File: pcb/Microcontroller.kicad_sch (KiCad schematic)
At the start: 36 parts, among them J1 ISP, Q2 BC817, Q3 BC817, Q4 BC817, SW2 RESET, SW3 START, SW4 STOP, U4 ATmega328P-A, Y1 15MHz

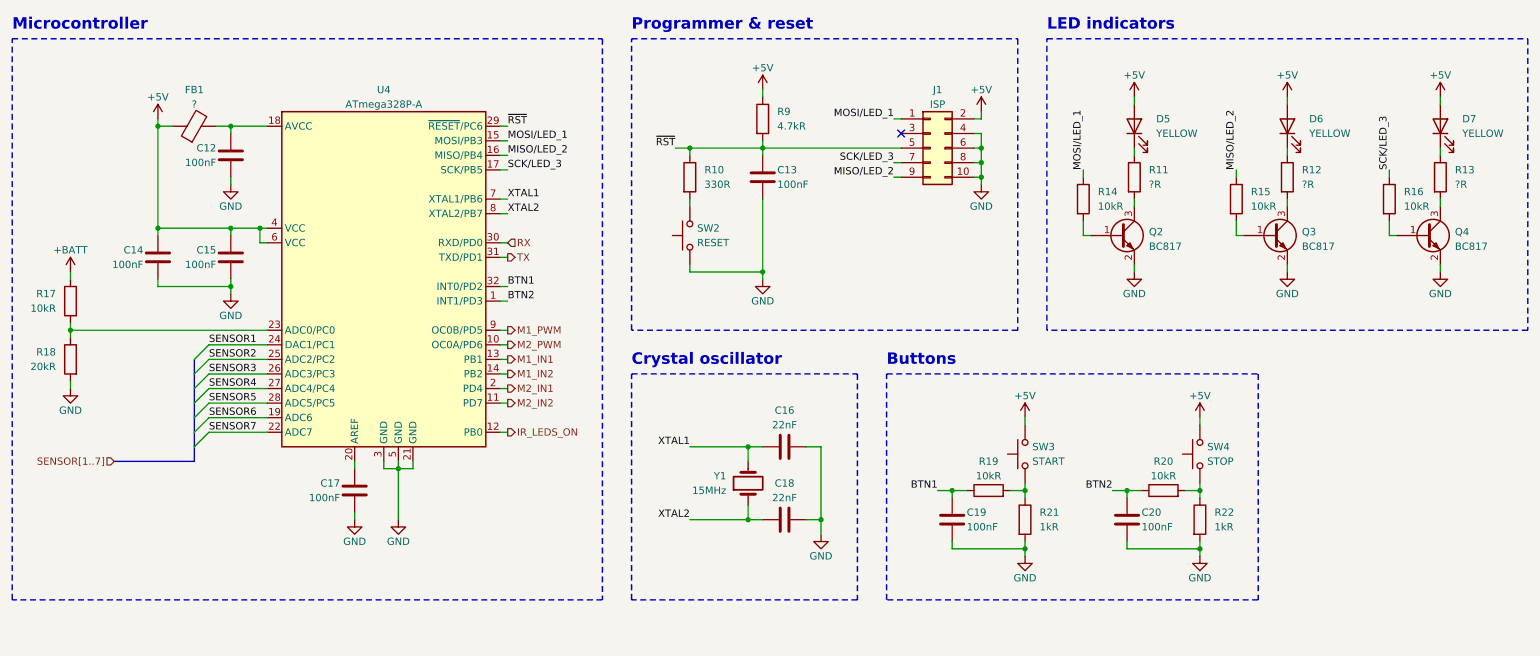
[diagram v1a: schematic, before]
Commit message: [pcb] Schematic clean-up
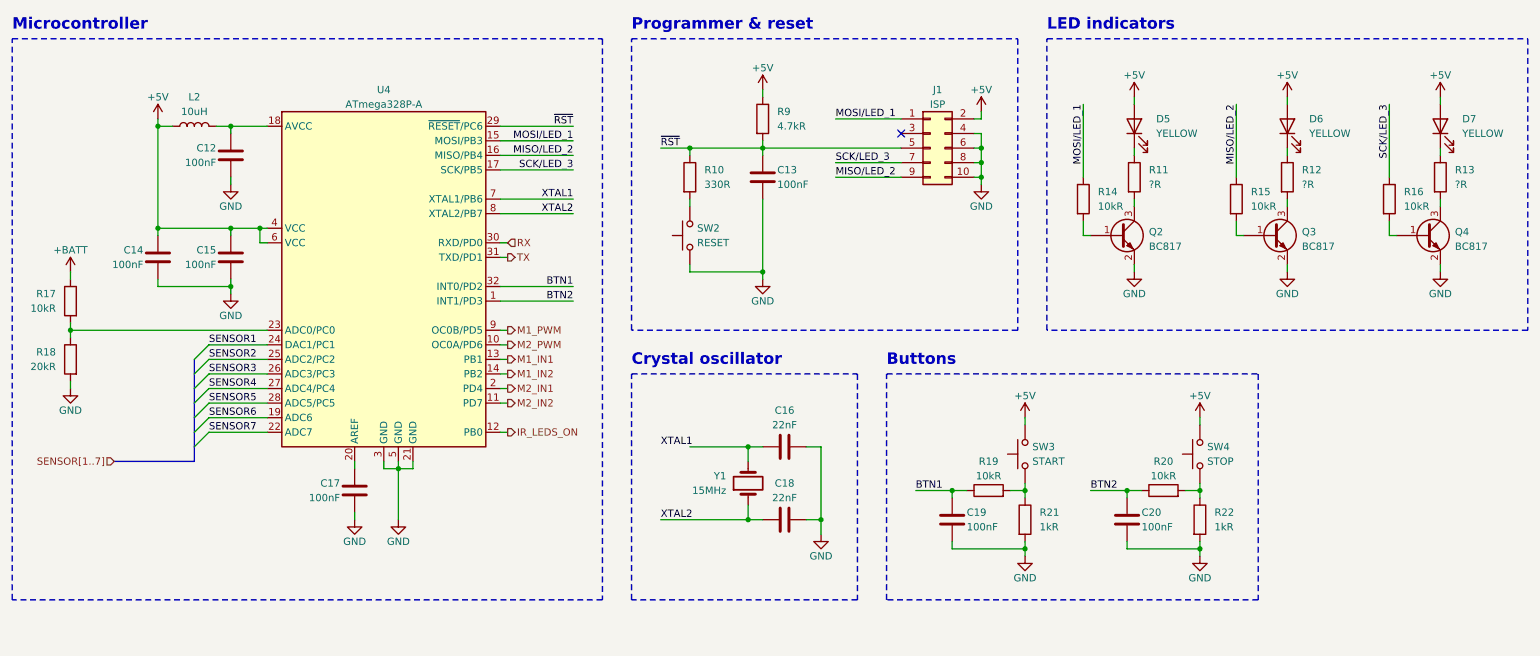
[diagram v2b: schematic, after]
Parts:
- removed FB1: ?, symbol Device:FerriteBead
- added L2: 10uH, symbol Device:L
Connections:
- net +5V: now also L2.1
- net XTAL1: no longer C16.1, Y1.2
- net at C12.1, U4.18 (AVCC): now also L2.2
- new net: C16.1, Y1.2

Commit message: [pcb] Footprints assigned
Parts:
- C12, C13, C14, C15, C16, C17, C18, C19, C20: footprint (none) -> Capacitor_SMD:C_0805_2012Metric
- D5, D6, D7: footprint (none) -> LED_SMD:LED_0805_2012Metric
- L2: footprint (none) -> Inductor_SMD:L_0805_2012Metric
- R10, R11, R12, R13, R14, R15, R16, R17, R18, R19, R20, R21, R22, R9: footprint (none) -> Resistor_SMD:R_0805_2012Metric
- SW2, SW3, SW4: footprint (none) -> Button_Switch_THT:SW_PUSH_6mm_H5mm
- Y1: footprint (none) -> Crystal:Crystal_HC49-4H_Vertical
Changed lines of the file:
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@@
       (effects (font (size 1.27 1.27)) (justify left))
     )
-    (property "Footprint" "" (at 75.2348 101.6 0)
+    (property "Footprint" "Capacitor_SMD:C_0805_2012Metric" (at 75.2348 101.6 0)
       (effects (font (size 1.27 1.27)) hide)
     )
@@
       (effects (font (size 1.27 1.27)) (justify right))
     )
-    (property "Footprint" "" (at 187.96 91.44 0)
+    (property "Footprint" "Button_Switch_THT:SW_PUSH_6mm_H5mm" (at 187.96 91.44 0)
       (effects (font (size 1.27 1.27)) hide)
     )
@@
       (effects (font (size 1.27 1.27)) (justify right))
     )
-    (property "Footprint" "" (at 212.09 34.29 0)
+    (property "Footprint" "LED_SMD:LED_0805_2012Metric" (at 212.09 34.29 0)
       (effects (font (size 1.27 1.27)) hide)
     )
@@
       (effects (font (size 1.27 1.27)) (justify left))
     )
-    (property "Footprint" "" (at 144.78 96.52 0)
+    (property "Footprint" "Crystal:Crystal_HC49-4H_Vertical" (at 144.78 96.52 0)
       (effects (font (size 1.27 1.27)) hide)
     )
@@
       (effects (font (size 1.27 1.27)))
     )
-    (property "Footprint" "" (at 217.17 99.568 90)
+    (property "Footprint" "Resistor_SMD:R_0805_2012Metric" (at 217.17 99.568 90)
       (effects (font (size 1.27 1.27)) hide)
     )
@@
       (effects (font (size 1.27 1.27)) (justify right))
     )
-    (property "Footprint" "" (at 129.54 53.34 0)
+    (property "Footprint" "Button_Switch_THT:SW_PUSH_6mm_H5mm" (at 129.54 53.34 0)
       (effects (font (size 1.27 1.27)) hide)
     )
@@
       (effects (font (size 1.27 1.27)) (justify right))
     )
-    (property "Footprint" "" (at 265.43 34.29 0)
+    (property "Footprint" "LED_SMD:LED_0805_2012Metric" (at 265.43 34.29 0)
       (effects (font (size 1.27 1.27)) hide)
     )
@@
       (effects (font (size 1.27 1.27)) (justify left))
     )
-    (property "Footprint" "" (at 53.6448 60.96 0)
+    (property "Footprint" "Capacitor_SMD:C_0805_2012Metric" (at 53.6448 60.96 0)
       (effects (font (size 1.27 1.27)) hide)
     )
@@
       (effects (font (size 1.27 1.27)))
     )
-    (property "Footprint" "" (at 48.26 34.29 0)
+    (property "Footprint" "Inductor_SMD:L_0805_2012Metric" (at 48.26 34.29 0)
       (effects (font (size 1.27 1.27)) hide)
     )
@@
       (effects (font (size 1.27 1.27)) (justify left))
     )
-    (property "Footprint" "" (at 221.742 102.87 90)
+    (property "Footprint" "Resistor_SMD:R_0805_2012Metric" (at 221.742 102.87 90)
       (effects (font (size 1.27 1.27)) hide)
     )
@@
       (effects (font (size 1.27 1.27)) (justify left))
     )
-    (property "Footprint" "" (at 228.092 46.99 90)
+    (property "Footprint" "Resistor_SMD:R_0805_2012Metric" (at 228.092 46.99 90)
       (effects (font (size 1.27 1.27)) hide)
     )
@@
       (effects (font (size 1.27 1.27)) (justify left))
     )
-    (property "Footprint" "" (at 191.262 102.87 90)
+    (property "Footprint" "Resistor_SMD:R_0805_2012Metric" (at 191.262 102.87 90)
       (effects (font (size 1.27 1.27)) hide)
     )
@@
       (effects (font (size 1.27 1.27)) (justify left))
     )
-    (property "Footprint" "" (at 211.7852 106.68 0)
+    (property "Footprint" "Capacitor_SMD:C_0805_2012Metric" (at 211.7852 106.68 0)
       (effects (font (size 1.27 1.27)) hide)
     )
@@
       (effects (font (size 1.27 1.27)) (justify left))
     )
-    (property "Footprint" "" (at 263.652 43.18 90)
+    (property "Footprint" "Resistor_SMD:R_0805_2012Metric" (at 263.652 43.18 90)
       (effects (font (size 1.27 1.27)) hide)
     )
@@
       (effects (font (size 1.27 1.27)) (justify left))
     )
-    (property "Footprint" "" (at 145.542 33.02 90)
+    (property "Footprint" "Resistor_SMD:R_0805_2012Metric" (at 145.542 33.02 90)
       (effects (font (size 1.27 1.27)) hide)
     )
@@
       (effects (font (size 1.27 1.27)))
     )
-    (property "Footprint" "" (at 186.69 99.568 90)
+    (property "Footprint" "Resistor_SMD:R_0805_2012Metric" (at 186.69 99.568 90)
       (effects (font (size 1.27 1.27)) hide)
     )
@@
       (effects (font (size 1.27 1.27)) (justify left))
     )
-    (property "Footprint" "" (at 53.6448 43.18 0)
+    (property "Footprint" "Capacitor_SMD:C_0805_2012Metric" (at 53.6448 43.18 0)
       (effects (font (size 1.27 1.27)) hide)
     )
@@
       (effects (font (size 1.27 1.27)) (justify left))
     )
-    (property "Footprint" "" (at 148.2852 46.99 0)
+    (property "Footprint" "Capacitor_SMD:C_0805_2012Metric" (at 148.2852 46.99 0)
       (effects (font (size 1.27 1.27)) hide)
     )
@@
       (effects (font (size 1.27 1.27)) (justify left))
     )
-    (property "Footprint" "" (at 181.3052 106.68 0)
+    (property "Footprint" "Capacitor_SMD:C_0805_2012Metric" (at 181.3052 106.68 0)
       (effects (font (size 1.27 1.27)) hide)
     )
@@
       (effects (font (size 1.27 1.27)) (justify left))
     )
-    (property "Footprint" "" (at 28.448 64.77 90)
+    (property "Footprint" "Resistor_SMD:R_0805_2012Metric" (at 28.448 64.77 90)
       (effects (font (size 1.27 1.27)) hide)
     )
@@
       (effects (font (size 1.27 1.27)) (justify left))
     )
-    (property "Footprint" "" (at 40.9448 60.96 0)
+    (property "Footprint" "Capacitor_SMD:C_0805_2012Metric" (at 40.9448 60.96 0)
       (effects (font (size 1.27 1.27)) hide)
     )
@@
       (effects (font (size 1.27 1.27)) (justify left))
     )
-    (property "Footprint" "" (at 132.842 43.18 90)
+    (property "Footprint" "Resistor_SMD:R_0805_2012Metric" (at 132.842 43.18 90)
       (effects (font (size 1.27 1.27)) hide)
     )
@@
       (effects (font (size 1.27 1.27)))
     )
-    (property "Footprint" "" (at 154.94 89.2048 0)
+    (property "Footprint" "Capacitor_SMD:C_0805_2012Metric" (at 154.94 89.2048 0)
       (effects (font (size 1.27 1.27)) hide)
     )
@@
       (effects (font (size 1.27 1.27)) (justify left))
     )
-    (property "Footprint" "" (at 28.448 74.93 90)
+    (property "Footprint" "Resistor_SMD:R_0805_2012Metric" (at 28.448 74.93 90)
       (effects (font (size 1.27 1.27)) hide)
     )
@@
       (effects (font (size 1.27 1.27)))
     )
-    (property "Footprint" "" (at 154.94 101.9048 0)
+    (property "Footprint" "Capacitor_SMD:C_0805_2012Metric" (at 154.94 101.9048 0)
       (effects (font (size 1.27 1.27)) hide)
     )
@@
       (effects (font (size 1.27 1.27)) (justify left))
     )
-    (property "Footprint" "" (at 201.422 46.99 90)
+    (property "Footprint" "Resistor_SMD:R_0805_2012Metric" (at 201.422 46.99 90)
       (effects (font (size 1.27 1.27)) hide)
     )
@@
       (effects (font (size 1.27 1.27)) (justify right))
     )
-    (property "Footprint" "" (at 238.76 34.29 0)
+    (property "Footprint" "LED_SMD:LED_0805_2012Metric" (at 238.76 34.29 0)
       (effects (font (size 1.27 1.27)) hide)
     )
@@
       (effects (font (size 1.27 1.27)) (justify left))
     )
-    (property "Footprint" "" (at 210.312 43.18 90)
+    (property "Footprint" "Resistor_SMD:R_0805_2012Metric" (at 210.312 43.18 90)
       (effects (font (size 1.27 1.27)) hide)
     )
@@
       (effects (font (size 1.27 1.27)) (justify right))
     )
-    (property "Footprint" "" (at 218.44 91.44 0)
+    (property "Footprint" "Button_Switch_THT:SW_PUSH_6mm_H5mm" (at 218.44 91.44 0)
       (effects (font (size 1.27 1.27)) hide)
     )
@@
       (effects (font (size 1.27 1.27)) (justify left))
     )
-    (property "Footprint" "" (at 254.762 46.99 90)
+    (property "Footprint" "Resistor_SMD:R_0805_2012Metric" (at 254.762 46.99 90)
       (effects (font (size 1.27 1.27)) hide)
     )
@@
       (effects (font (size 1.27 1.27)) (justify left))
     )
-    (property "Footprint" "" (at 236.982 43.18 90)
-      (effects (font (size 1.27 1.27)) hide)
-    )
+    (property "Footprint" "Resistor_SMD:R_0805_2012Metric" (at 236.982 43.18 90)
+      (effects (font (size 1.27 1.27)) hide)
+    )

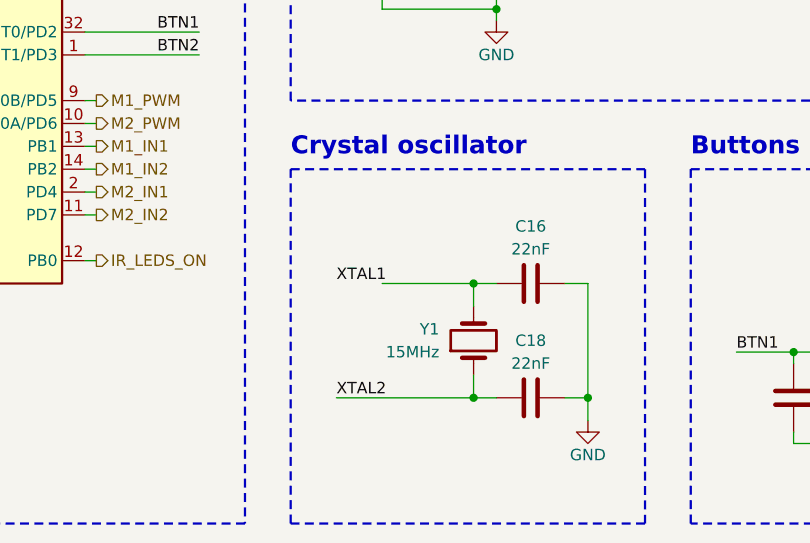
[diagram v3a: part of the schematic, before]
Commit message: [pcb] Missing connection
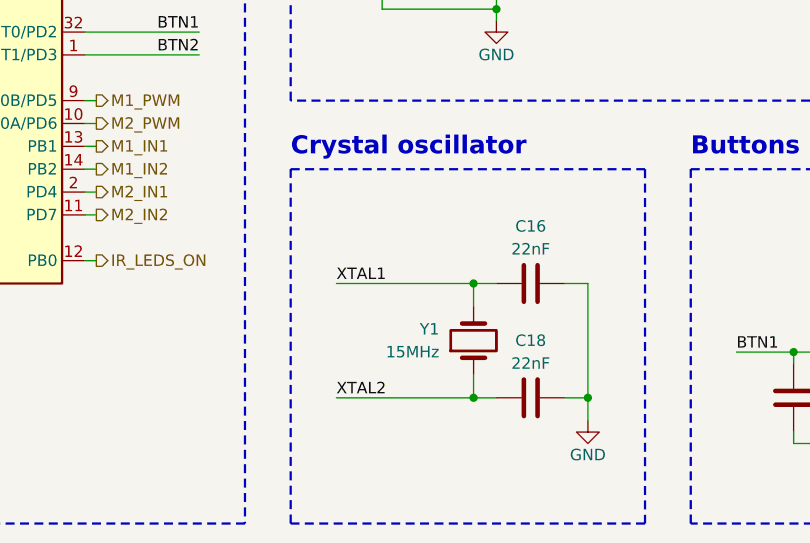
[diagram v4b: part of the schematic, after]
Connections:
- net XTAL1: now also C16.1, Y1.2
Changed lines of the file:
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@@
     (stroke (width 0) (type default))
   )
-  (wire (pts (xy 134.62 90.17) (xy 144.78 90.17))
+  (wire (pts (xy 129.54 90.17) (xy 144.78 90.17))
     (stroke (width 0) (type default))
   )
